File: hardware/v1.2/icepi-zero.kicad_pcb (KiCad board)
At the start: 4 copper layers, 65 x 30 mm, 156 parts, among them J1 Conn_02x20_Counter_Clockwise, J2 HDMI_C_1.3, J3 USB_C_Receptacle_USB2.0_14P, J4 USB_C_Receptacle_USB2.0_14P, J5 USB_C_Receptacle_USB2.0_14P, J6 Micro_SD_Card_Det2, SW1 SW_Push, SW2 SW_Push, U1 ECP5U_25F_CABGA256, U10 W9825G6KH, U11 W25Q128JVS, U2 TLV62569DBV, U3 TLV62569DBV, U4 TLV62569DBV, U5 PCA9306DC1, U6 FT231XQ, U7 TPD2EUSB30A, U8 TPD2EUSB30A, U9 TPD2EUSB30A, Y1 SITxxxxxx-1x-33E-50.000000

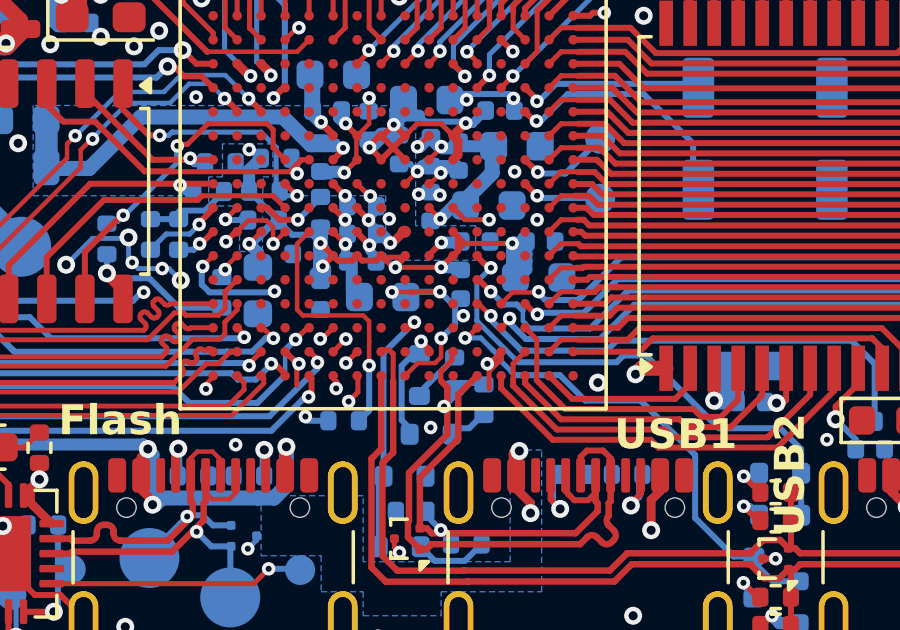
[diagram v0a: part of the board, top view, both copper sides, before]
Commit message: Fix typo in README
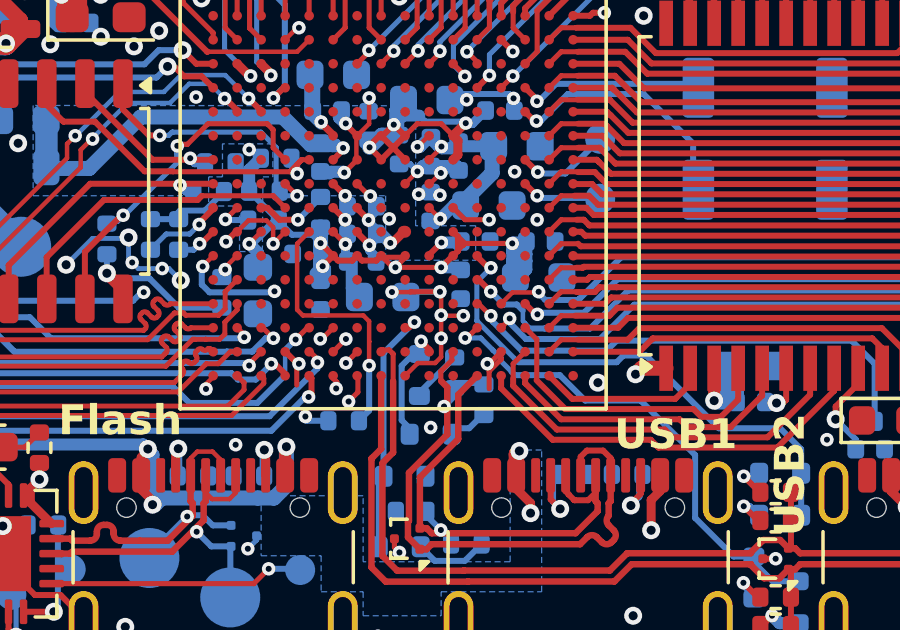
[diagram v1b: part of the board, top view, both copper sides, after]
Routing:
- net GND: track 85.9 -> 86.2 mm, vias 108 -> 109
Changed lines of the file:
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@@
+	)
+	(segment
+		(start 152.34004 108.75)
+		(end 151.62 108.75)
+		(width 0.15)
+		(layer "F.Cu")
+		(net 31)
 	)
 	(segment
@@
 	)
 	(segment
+		(start 151.62 108.75)
+		(end 151.6 108.77)
+		(width 0.15)
+		(layer "F.Cu")
+		(net 31)
+	)
+	(segment
 		(start 148.8 102.75)
 		(end 148.42 102.37)
@@
 	)
 	(segment
+		(start 151.6 108.77)
+		(end 151.6 109.5)
+		(width 0.15)
+		(layer "F.Cu")
+		(net 31)
+	)
+	(segment
 		(start 124.575 108.0375)
 		(end 127 108.0375)
@@
 	)
 	(segment
+		(start 151.6 107.99)
+		(end 151.6 108.73)
+		(width 0.15)
+		(layer "F.Cu")
+		(net 31)
+	)
+	(segment
 		(start 146.41 109.95)
 		(end 146.809999 110.349999)
@@
 	)
 	(segment
+		(start 151.6 108.73)
+		(end 151.6 108.77)
+		(width 0.15)
+		(layer "F.Cu")
+		(net 31)
+	)
+	(segment
 		(start 136.67 119.43)
 		(end 136.69 119.45)
@@
 	)
 	(segment
+		(start 151.56 107.95)
+		(end 151.6 107.99)
+		(width 0.15)
+		(layer "F.Cu")
+		(net 31)
+	)
+	(segment
 		(start 153.6 110.2)
 		(end 153.2 110.6)
@@
 		(layers "F.Cu" "B.Cu")
 		(free yes)
+		(net 31)
+	)
+	(via
+		(at 151.6 108.73)
+		(size 0.45)
+		(drill 0.2)
+		(layers "F.Cu" "B.Cu")
 		(net 31)
 	)
@@
 	)
 	(segment
-		(start 151.56 107.95)
-		(end 152.066 108.456)
-		(width 0.2)
-		(layer "B.Cu")
-		(net 31)
-	)
-	(segment
 		(start 151.21 103.76)
 		(end 150.99 103.76)
@@
 	)
 	(segment
-		(start 152.066 108.456)
-		(end 152.066 109.034)
-		(width 0.2)
-		(layer "B.Cu")
-		(net 31)
-	)
-	(segment
 		(start 149.905775 106.323234)
 		(end 149.602541 106.02)
@@
 		(layer "B.Cu")
 		(net 31)
-	)
-	(segment
-		(start 152.066 109.034)
-		(end 151.6 109.5)
-		(width 0.2)
-		(layer "B.Cu")
-		(net 31)

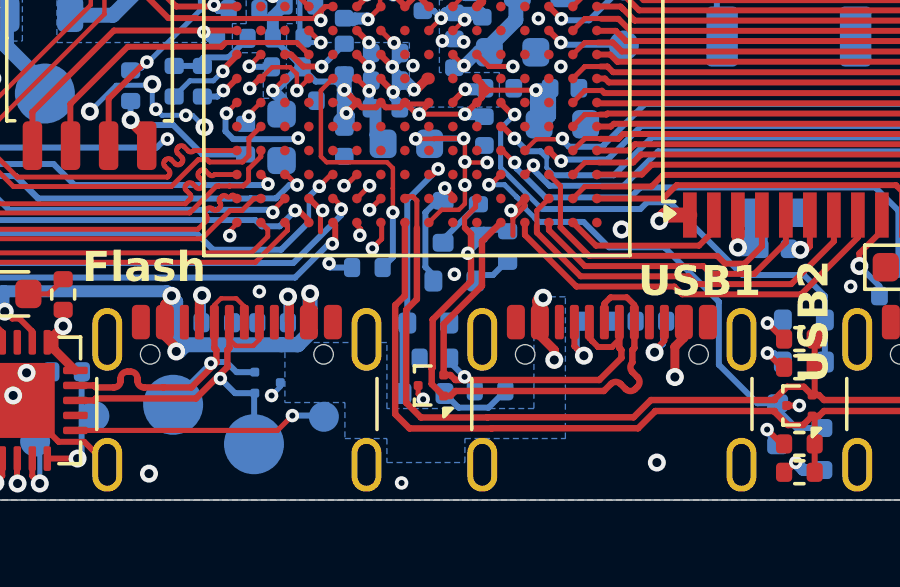
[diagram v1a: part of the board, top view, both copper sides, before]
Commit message: Update pic on readme
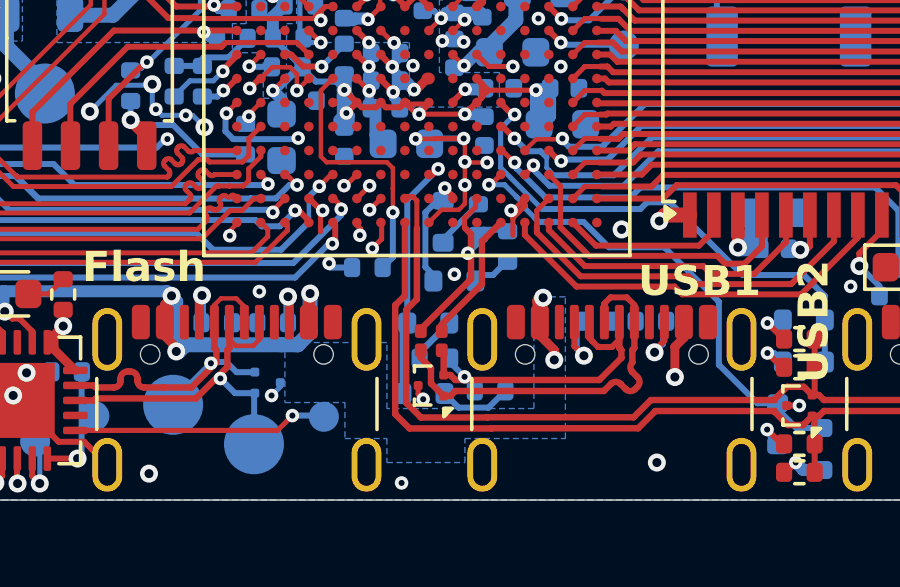
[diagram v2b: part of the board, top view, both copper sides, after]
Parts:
- added R41: 27, Resistor_SMD:R_0201_0603Metric, F.Cu at (150.8, 114.7)
- added R42: 27, Resistor_SMD:R_0201_0603Metric, F.Cu at (150.1, 114.7)
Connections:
- J5 pad A6: D2+ -> Net-(U9-D+)
- J5 pad A7: D2- -> Net-(U9-D-)
- J5 pad B6: D2+ -> Net-(U9-D+)
- J5 pad B7: D2- -> Net-(U9-D-)
- R40 pad 2: D2- -> Net-(U9-D-)
- R43 pad 2: D2- -> Net-(U9-D-)
- U9 pad 1: D2+ -> Net-(U9-D+)
- U9 pad 2: D2- -> Net-(U9-D-)
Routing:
- net D2+: track 20.8 -> 7.12 mm
- net Net-(U9-D+): track 0.00 -> 13.3 mm
- net D2-: track 17.1 -> 4.44 mm, vias 1 -> 0
- net Net-(U9-D-): track 0.00 -> 12.0 mm, vias 0 -> 1
- net Net-(D7-A): track 0.00 -> 1.58 mm
